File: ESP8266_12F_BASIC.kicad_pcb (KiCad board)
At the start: 2 copper layers, 64.7 x 63.5 mm, 34 parts, among them J1 Conn_01x02_Male, Q1 BC547, U1 ESP-12F, U2 AP1117-33

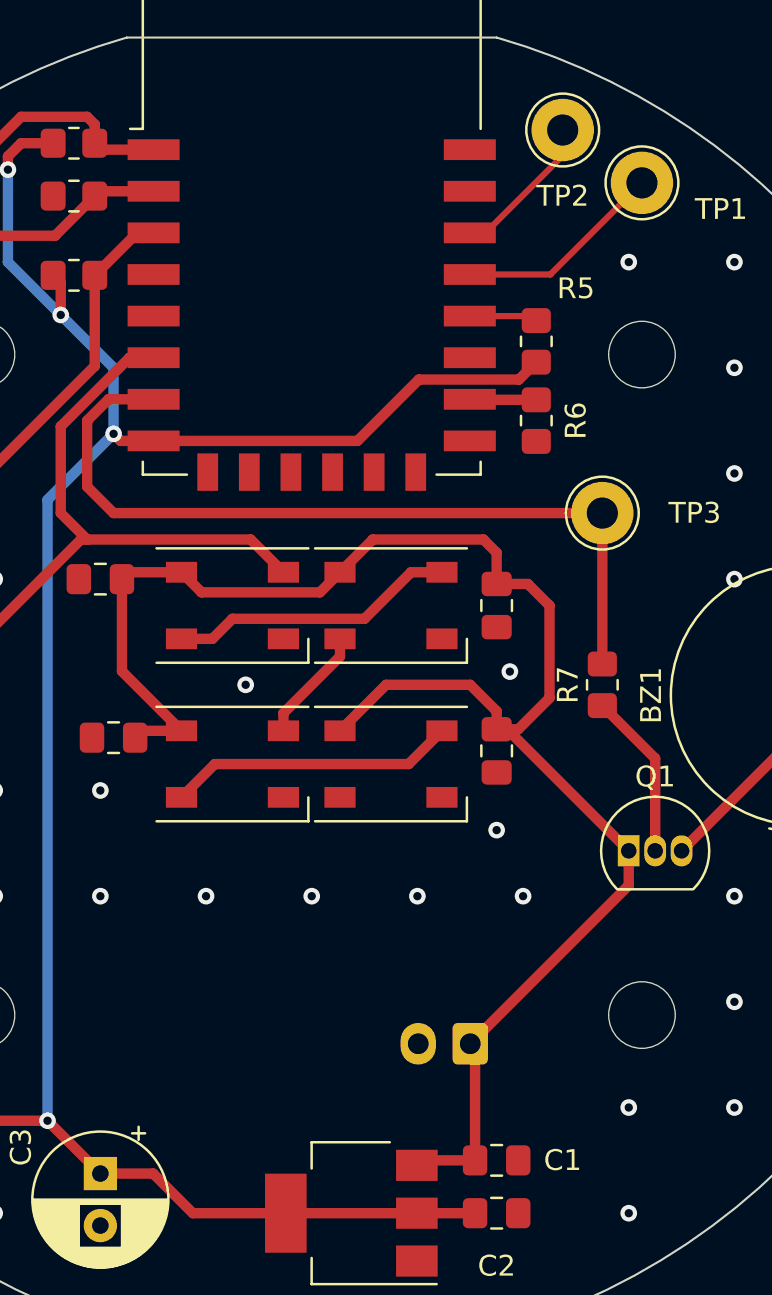
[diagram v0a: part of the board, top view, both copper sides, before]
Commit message: fixed header position
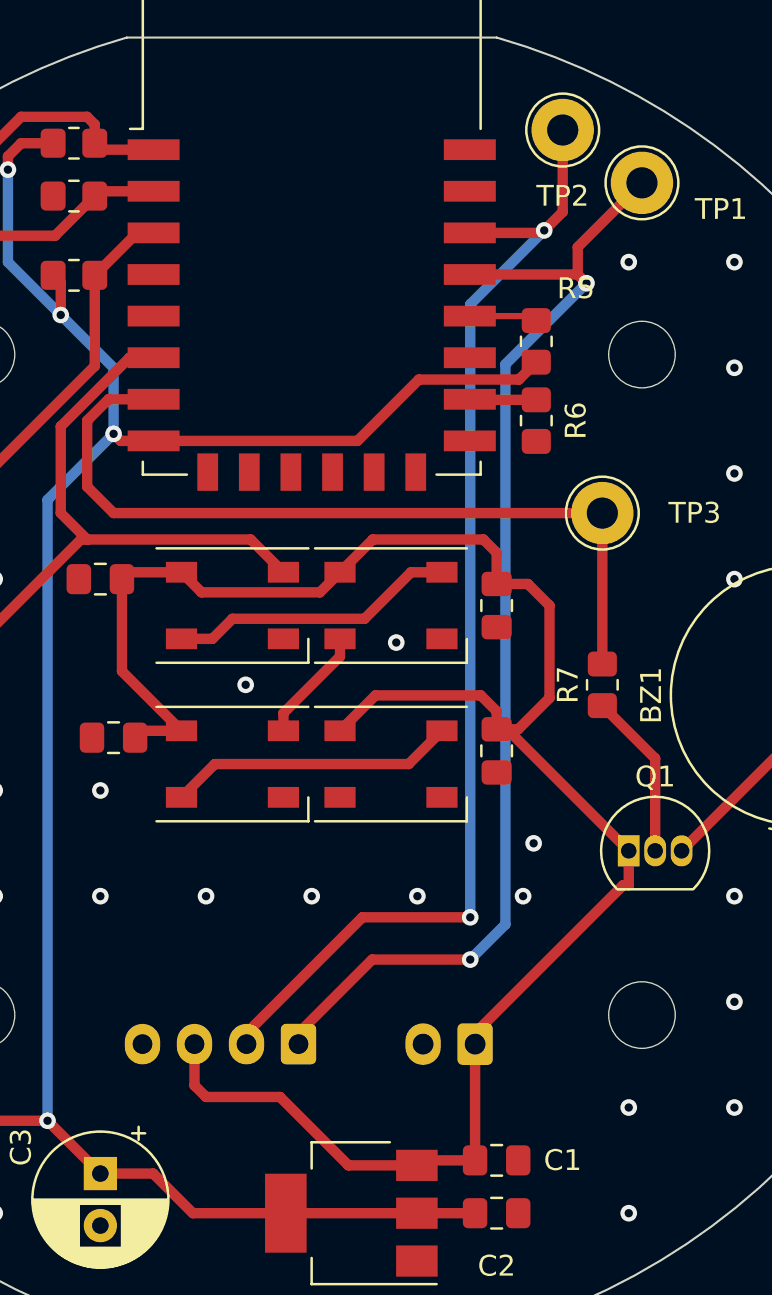
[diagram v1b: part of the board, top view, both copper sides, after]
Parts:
- added J2: Conn_01x04_Male, Connector_JST:JST_XH_B4B-XH-A_1x04_P2.50mm_Vertical, B.Cu at (151.8, 118.9)
- moved J1 0.23 mm to (160.3, 118.9)
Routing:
- net MHZ_RX: track 7.23 -> 56.4 mm, vias 0 -> 2
- net MHZ_TX: track 10.1 -> 56.0 mm, vias 0 -> 2
- net VCC_IN: track 82.4 -> 96.8 mm

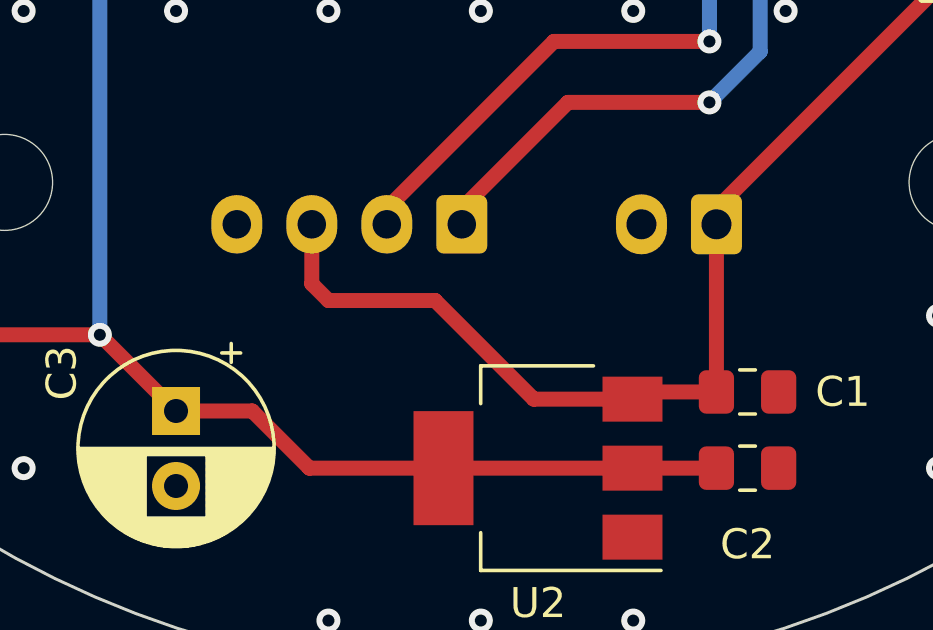
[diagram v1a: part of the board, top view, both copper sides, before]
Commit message: added silkscreen for header
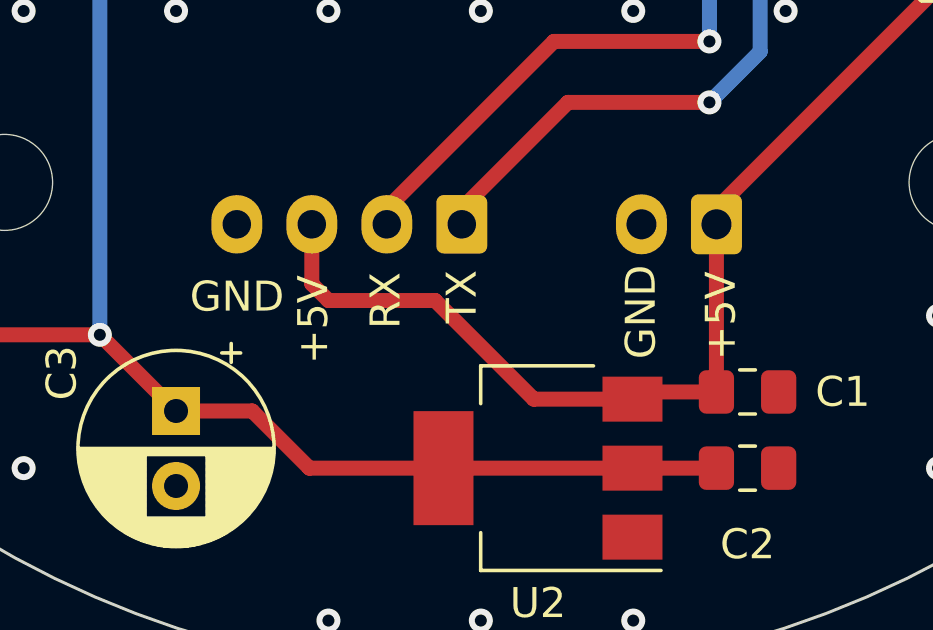
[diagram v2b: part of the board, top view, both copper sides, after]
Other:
- board text added: "+5V"
- board text added: "GND"
- board text added: "RX"
- board text added: "TX"
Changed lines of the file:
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@@
   (gr_line (start 143.51 70.485) (end 161.29 70.485) (layer "Edge.Cuts") (width 0.1))
   (gr_arc (start 161.29 70.485) (mid 152.4 133.960088) (end 143.51 70.485) (layer "Edge.Cuts") (width 0.1))
+  (gr_text "TX" (at 151.765 121.285 90) (layer "F.SilkS")
+    (effects (font (size 1 1) (thickness 0.15)))
+  )
+  (gr_text "RX" (at 149.225 121.412 90) (layer "F.SilkS")
+    (effects (font (size 1 1) (thickness 0.15)))
+  )
+  (gr_text "GND" (at 144.272 121.285) (layer "F.SilkS")
+    (effects (font (size 1 1) (thickness 0.15)))
+  )
+  (gr_text "+5V" (at 160.401 121.92 90) (layer "F.SilkS")
+    (effects (font (size 1 1) (thickness 0.15)))
+  )
+  (gr_text "+5V" (at 146.812 122.047 90) (layer "F.SilkS")
+    (effects (font (size 1 1) (thickness 0.15)))
+  )
+  (gr_text "GND" (at 157.734 121.793 90) (layer "F.SilkS")
+    (effects (font (size 1 1) (thickness 0.15)))
+  )
   (segment (start 175.895 104.605785) (end 175.154215 104.605785) (width 0.5) (layer "F.Cu") (net 1))
   (segment (start 175.154215 104.605785) (end 170.18 109.58) (width 0.5) (layer "F.Cu") (net 1))
